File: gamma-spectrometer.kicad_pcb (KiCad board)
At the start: 2 copper layers, 123.5 x 49.5 mm, 79 parts, among them J1 *, J2 *, J3 20449-001E-03, J4 *, J5 20449-001E-03, J6 *, Q1 2N7002, Q2 2N7002, Q3 MMBT5088LT1G, Q4 MMBT5088LT1G, SW1 *, U1 Pico 2, U10 MICROFC-60035-SMT-TR1, U2 OPA357AIDBVR, U3 TLV3201AIDBVR, U4 OPA357AIDBVR, U5 OPA357AIDBVR, U6 LM4040AIM3-3.0+T, U7 LM4040AIM3-3.0+T, U8 MAX5026EUT_T, U9 TPS7B6950DBVR

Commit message: BDG4-01 module boards design
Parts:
- removed J3, J5: 20449-001E-03, 20449-001E-03:IPEX_20449-001E-03
- removed J4, J6: *, B2B-PH-K-S_LF__SN_:JST_B2B-PH-K-S(LF)(SN)
- removed LS1: AST0760MCTRQ (6kHz), AST0760MCTRQ:AST0760_MAL
- removed Q2: 2N7002, Package_TO_SOT_SMD:SOT-23
- removed SW1: *, SW_TL3305AF160QG:SW_TL3305AF160QG
- C10, C11, C12, C13, C14, C15, C16, C18, C4, C5, C6, C8, C9, D3, D5, FB2, FB3, L1, Q1, R10, R11, R12, R13, R14, R15, R16, R6, R9, U4, U5, U6, U8: moved to B.Cu
- R1: value 1k -> 210k
- R2: value 100R -> 1k
- R4: value 210k -> 1k; moved to B.Cu
- R5: value 1k -> 100R
- R7: value 1k -> 210k; moved to B.Cu
- R8: value 210k -> 1k
- VR1: value 5k -> 50k; footprint 3296W-1-502LF:TRIM_3296W-1-502LF -> 3296W-1-503LF:TRIM_3296W-1-503LF
- VR2: value 50k -> 5k; footprint 3296W-1-503LF:TRIM_3296W-1-503LF -> 3296W-1-502LF:TRIM_3296W-1-502LF
- moved VR1 38.9 mm to (155.0, 72.5), turned to 0 degrees
- moved C9 38.1 mm to (105.5, 84.1), turned to 180 degrees
- moved C10 36.5 mm to (105.5, 82.1), turned to 0 degrees
- moved U7 35.5 mm to (143.2, 79.2), turned to 90 degrees
- moved R3 35.0 mm to (154.2, 80.8), turned to -90 degrees
- moved R11 34.9 mm to (111.5, 85.5)
- moved JP2 33.7 mm to (120.5, 69.5), turned to 180 degrees
- moved R2 33.6 mm to (155.8, 80.8)
- moved U5 32.3 mm to (109.0, 81.8), turned to -90 degrees
- moved R1 32.2 mm to (152.8, 80.8)
- moved C8 31.6 mm to (111.5, 80.0), turned to -90 degrees
- moved R10 28.9 mm to (120.6, 84.2), turned to -90 degrees
- moved U2 28.6 mm to (147.2, 77.0), turned to 0 degrees
- moved D1 28.2 mm to (148.5, 80.8)
- moved D3 27.8 mm to (118.0, 83.4), turned to -90 degrees
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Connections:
- C11 pad 1: Net-(U8-VCC) -> Net-(D5-A)
- C6 pad 1: GND -> Net-(U3-IN-)
- C6 pad 2: VCC -> GND
- C7 pad 1: Net-(U3-IN-) -> GND
- C7 pad 2: GND -> VCC
- FB3 pad 1: Net-(U8-VCC) -> Net-(D5-A)
- L1 pad 2: Net-(U8-VCC) -> Net-(D5-A)
- R1 pad 1: GND -> ANODE_IN
- R1 pad 2: ANODE_IN -> VREF1
- R13 pad 1: VREF1 -> VREF
- R2 pad 1: ANODE_IN -> GND
- R2 pad 2: Net-(D1-COM) -> ANODE_IN
- R3 pad 2: VREF -> VREF1
- R4 pad 1: ANODE_IN -> GND
- R4 pad 2: VREF -> Net-(U2--IN)
- R5 pad 1: GND -> ANODE_IN
- R5 pad 2: Net-(U2--IN) -> Net-(D1-COM)
- R7 pad 1: Net-(D2-PadA) -> Net-(VR1-CW)
- R7 pad 2: INT -> Net-(R7-Pad2)
- R8 pad 1: Net-(VR2-CCW) -> Net-(D2-PadA)
- R8 pad 2: Net-(R8-Pad2) -> INT
- R9 pad 1: VREF1 -> VREF
- R9 pad 2: Net-(R8-Pad2) -> Net-(R7-Pad2)
- U1 pad 10: TCKR -> unconnected-(U1-GPIO7-Pad10)_1
- U1 pad 19: Net-(U1-GPIO14) -> unconnected-(U1-GPIO14-Pad19)_1
- U1 pad 35: VREF -> VREF1
- U1 pad 40: unconnected-(U1-VBUS-Pad40) -> VBUS
- U6 pad 1: VREF1 -> VREF
- U7 pad 1: VREF -> VREF1
- U8 pad 4: Net-(U8-VCC) -> Net-(D5-A)
- U8 pad 5: Net-(U8-VCC) -> Net-(D5-A)
- VR1 pad 1: SIG -> GND
- VR1 pad 2: SIG -> Net-(U3-IN-)
- VR1 pad 3: Net-(U2--IN) -> Net-(VR1-CW)
- VR2 pad 1: Net-(VR2-CCW) -> SIG
- VR2 pad 2: Net-(U3-IN-) -> SIG
- VR2 pad 3: GND -> Net-(U2--IN)
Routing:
- net GND: track 151.7 -> 49.2 mm
- net VREF1: track 14.2 -> 62.6 mm, vias 0 -> 1
- net PEAK: track 56.2 -> 13.6 mm
- net TCKR: track 35.5 -> 0.00 mm
- net VREF: track 34.5 -> 3.69 mm, vias 3 -> 0
- net GND1: track 29.1 -> 0.00 mm, vias 0 -> 2
- net RST: track 29.9 -> 7.38 mm, vias 1 -> 0
- net +5V: track 93.2 -> 72.4 mm, vias 1 -> 2
- net SIG: track 39.7 -> 59.5 mm
- net VCC: track 134.0 -> 153.5 mm, vias 1 -> 2
- net Net-(U8-VCC): track 19.5 -> 0.00 mm
- net Net-(Q4-B): track 5.79 -> 24.9 mm
- net Net-(D5-A): track 9.71 -> 28.3 mm
- net PS_IN: track 14.1 -> 31.9 mm, vias 0 -> 1
- net Net-(U2--IN): track 25.4 -> 13.7 mm
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- added copper zone on F.Cu, net GND
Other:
- board size 123.5 x 49.5 mm -> 145.3 x 36.5 mm
- board text added: "CS"
- board text added: "GND"
- board text added: "MicroUSB"
- board text added: "OpenGammaKit v0.1.0"
- board text added: "RX"
- board text added: "SCK"
- board text added: "SCL"
- board text added: "SDA"
- board text added: "TX"
- board text added: "UR1"
- board text added: "UR2"
- board text added: "VCC"
- board text added: "БДГ4-01-А"
- board text added: "БДГ4-01-Б"
- board text removed: "Module v0.0.8"
- board text removed: "U2"

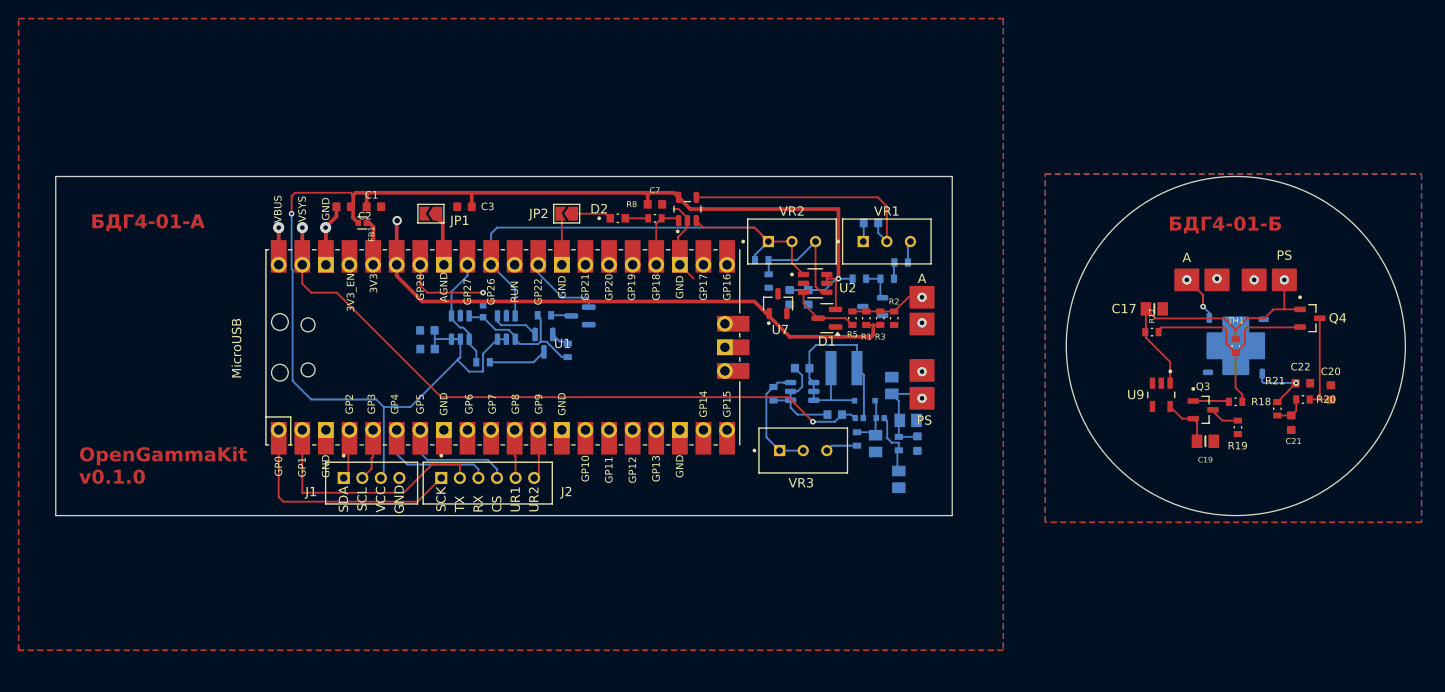
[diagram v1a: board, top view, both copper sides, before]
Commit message: PCB changes for more precise assembling
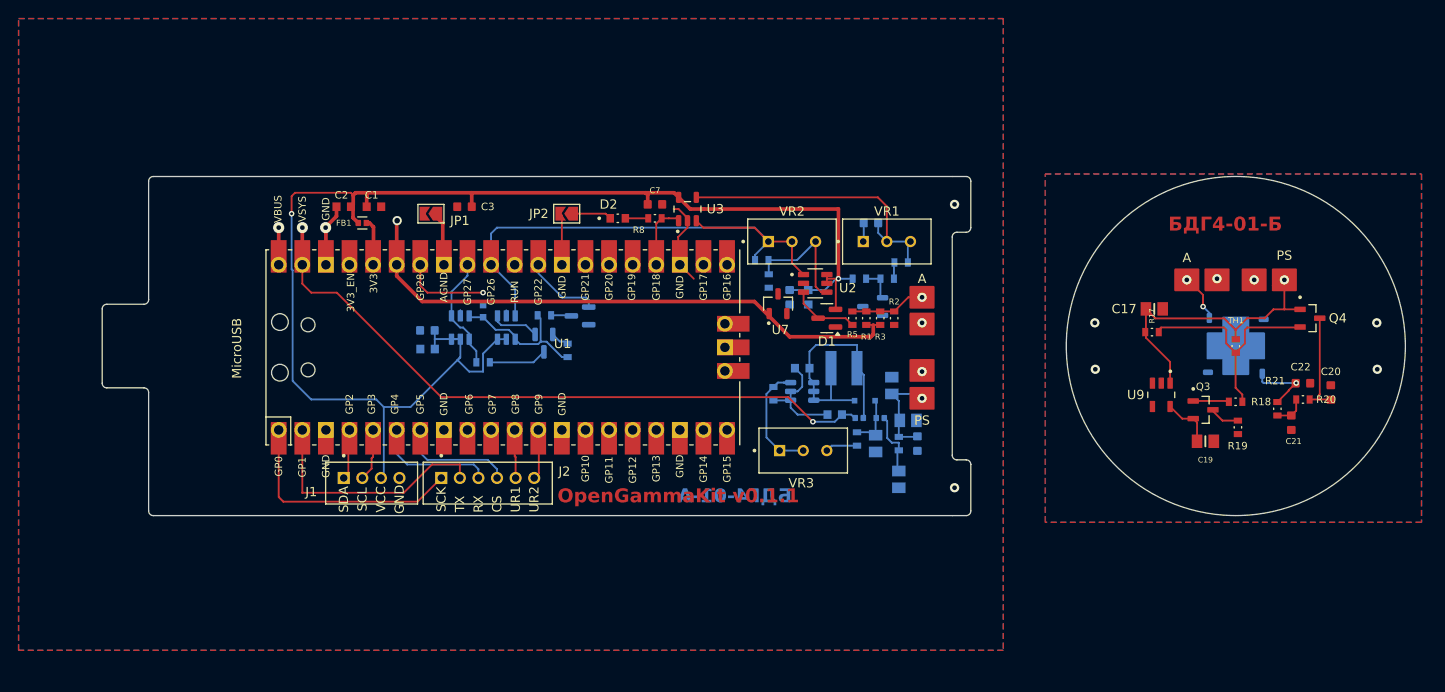
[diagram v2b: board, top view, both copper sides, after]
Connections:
- R7 pad 1: Net-(VR1-CW) -> Net-(U3-IN-)
- VR1 pad 3: Net-(VR1-CW) -> Net-(U3-IN-)
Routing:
- net Net-(U3-IN-): track 27.1 -> 32.0 mm
- net Net-(VR1-CW): track 2.36 -> 0.00 mm
- net GND1: vias 2 -> 6
- net GND: vias 4 -> 6
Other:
- board size 145.3 x 36.5 mm -> 140.3 x 36.5 mm
- board text added: "OpenGammaKit v0.1.1"
- board text removed: "OpenGammaKit v0.1.0"

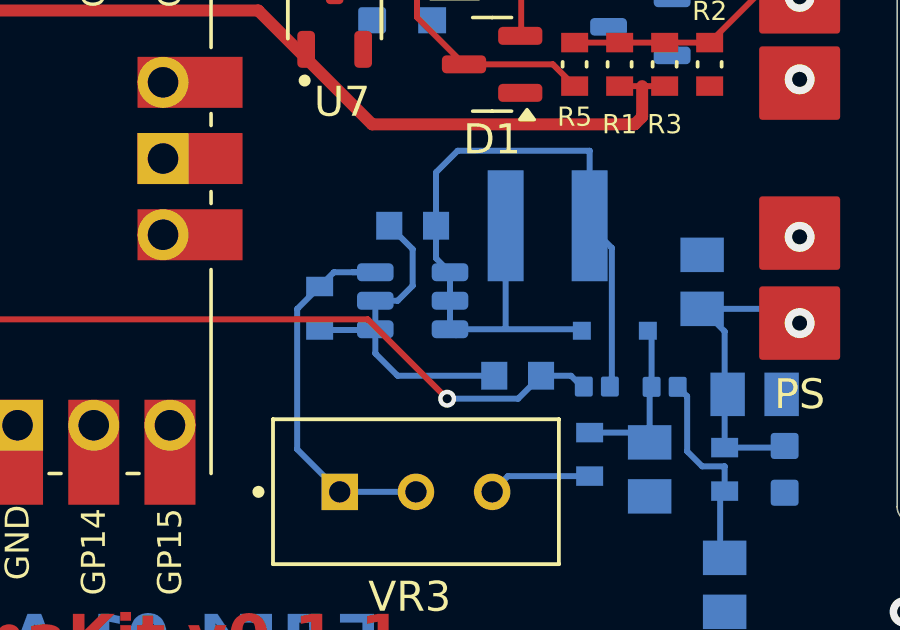
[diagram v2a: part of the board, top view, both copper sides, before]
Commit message: Important fix for SiPM power supply circuit. Moved gerber files.
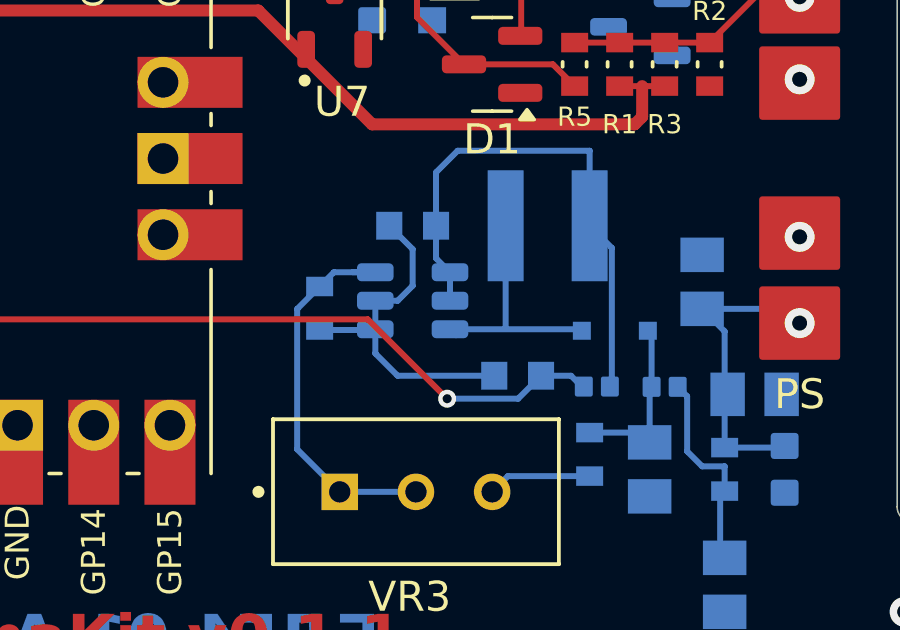
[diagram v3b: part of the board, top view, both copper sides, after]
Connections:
- C11 pad 1: Net-(D5-A) -> Net-(U8-VCC)
- FB3 pad 1: Net-(D5-A) -> Net-(U8-VCC)
- L1 pad 2: Net-(D5-A) -> Net-(U8-VCC)
- U8 pad 4: Net-(D5-A) -> Net-(U8-VCC)
- U8 pad 5: Net-(D5-A) -> Net-(U8-VCC)
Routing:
- net Net-(D5-A): track 28.3 -> 8.85 mm
- net Net-(U8-VCC): track 0.00 -> 18.5 mm
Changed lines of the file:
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@@
 			(drillshape 0)
 			(scaleselection 1)
-			(outputdirectory "gerber-files/")
+			(outputdirectory "fabrication-outputs/gerber-files/")
 		)
 	)
@@
 	(net 86 "unconnected-(U1-GPIO14-Pad19)_1")
 	(net 87 "VBUS")
+	(net 88 "Net-(U8-VCC)")
 	(footprint "3296W-1-503LF:TRIM_3296W-1-503LF"
 		(layer "F.Cu")
@@
 			(layers "B.Cu" "B.Paste" "B.Mask")
 			(roundrect_rratio 0.125)
-			(net 61 "Net-(D5-A)")
+			(net 88 "Net-(U8-VCC)")
 			(pintype "passive")
 			(solder_mask_margin 0.102)
@@
 			(size 0.87 0.93)
 			(layers "B.Cu" "B.Paste" "B.Mask")
-			(net 61 "Net-(D5-A)")
+			(net 88 "Net-(U8-VCC)")
 			(pintype "passive")
 			(solder_mask_margin 0.102)
@@
 			(layers "B.Cu" "B.Paste" "B.Mask")
 			(roundrect_rratio 0.25)
-			(net 61 "Net-(D5-A)")
+			(net 88 "Net-(U8-VCC)")
 			(pinfunction "~{SHDN}")
 			(pintype "input")
@@
 			(layers "B.Cu" "B.Paste" "B.Mask")
 			(roundrect_rratio 0.25)
-			(net 61 "Net-(D5-A)")
+			(net 88 "Net-(U8-VCC)")
 			(pinfunction "VCC")
 			(pintype "power_in")
@@
 			(size 1.2 3.7)
 			(layers "B.Cu" "B.Paste" "B.Mask")
-			(net 61 "Net-(D5-A)")
+			(net 88 "Net-(U8-VCC)")
 			(pintype "passive")
 			(solder_mask_margin 0.102)
@@
 	)
 	(segment
-		(start 146.63 87.215)
-		(end 147.095 87.68)
-		(width 0.2)
-		(layer "B.Cu")
-		(net 61)
-	)
-	(segment
-		(start 152.49 91.555)
-		(end 152.49 86.87)
-		(width 0.2)
-		(layer "B.Cu")
-		(net 61)
-	)
-	(segment
 		(start 148.95 86.13)
 		(end 148.95 89.48)
@@
 	)
 	(segment
-		(start 151.75 83.63)
-		(end 147.35 83.63)
-		(width 0.2)
-		(layer "B.Cu")
-		(net 61)
-	)
-	(segment
-		(start 147.095 87.68)
-		(end 147.4 87.68)
-		(width 0.2)
-		(layer "B.Cu")
-		(net 61)
-	)
-	(segment
-		(start 152.565 91.63)
-		(end 152.49 91.555)
-		(width 0.2)
-		(layer "B.Cu")
-		(net 61)
-	)
-	(segment
 		(start 147.095 89.58)
 		(end 151.44 89.58)
@@
 	)
 	(segment
-		(start 146.63 84.35)
-		(end 146.63 86.13)
-		(width 0.2)
-		(layer "B.Cu")
-		(net 61)
-	)
-	(segment
-		(start 147.35 83.63)
-		(end 146.63 84.35)
-		(width 0.2)
-		(layer "B.Cu")
-		(net 61)
-	)
-	(segment
-		(start 147.095 87.695)
-		(end 147.095 88.63)
-		(width 0.2)
-		(layer "B.Cu")
-		(net 61)
-	)
-	(segment
-		(start 146.63 86.13)
-		(end 146.63 87.215)
-		(width 0.2)
-		(layer "B.Cu")
-		(net 61)
-	)
-	(segment
 		(start 147.095 89.58)
 		(end 147.295 89.78)
@@
 	)
 	(segment
-		(start 151.75 86.13)
-		(end 151.75 83.63)
-		(width 0.2)
-		(layer "B.Cu")
-		(net 61)
-	)
-	(segment
-		(start 152.49 86.87)
-		(end 151.75 86.13)
-		(width 0.2)
-		(layer "B.Cu")
-		(net 61)
-	)
-	(segment
-		(start 147.095 88.63)
-		(end 147.095 89.58)
-		(width 0.2)
-		(layer "B.Cu")
-		(net 61)
-	)
-	(segment
-		(start 147.08 87.68)
-		(end 147.095 87.695)
-		(width 0.2)
-		(layer "B.Cu")
-		(net 61)
-	)
-	(segment
 		(start 153.75 91.565)
 		(end 153.815 91.5)
@@
 		(net 87)
 	)
+	(segment
+		(start 146.63 87.215)
+		(end 147.095 87.68)
+		(width 0.2)
+		(layer "B.Cu")
+		(net 88)
+	)
+	(segment
+		(start 152.49 91.555)
+		(end 152.49 86.87)
+		(width 0.2)
+		(layer "B.Cu")
+		(net 88)
+	)
+	(segment
+		(start 151.75 83.63)
+		(end 147.35 83.63)
+		(width 0.2)
+		(layer "B.Cu")
+		(net 88)
+	)
+	(segment
+		(start 147.095 87.68)
+		(end 147.4 87.68)
+		(width 0.2)
+		(layer "B.Cu")
+		(net 88)
+	)
+	(segment
+		(start 152.565 91.63)
+		(end 152.49 91.555)
+		(width 0.2)
+		(layer "B.Cu")
+		(net 88)
+	)
+	(segment
+		(start 146.63 84.35)
+		(end 146.63 86.13)
+		(width 0.2)
+		(layer "B.Cu")
+		(net 88)
+	)
+	(segment
+		(start 147.35 83.63)
+		(end 146.63 84.35)
+		(width 0.2)
+		(layer "B.Cu")
+		(net 88)
+	)
+	(segment
+		(start 147.095 87.695)
+		(end 147.095 88.63)
+		(width 0.2)
+		(layer "B.Cu")
+		(net 88)
+	)
+	(segment
+		(start 146.63 86.13)
+		(end 146.63 87.215)
+		(width 0.2)
+		(layer "B.Cu")
+		(net 88)
+	)
+	(segment
+		(start 151.75 86.13)
+		(end 151.75 83.63)
+		(width 0.2)
+		(layer "B.Cu")
+		(net 88)
+	)
+	(segment
+		(start 152.49 86.87)
+		(end 151.75 86.13)
+		(width 0.2)
+		(layer "B.Cu")
+		(net 88)
+	)
+	(segment
+		(start 147.08 87.68)
+		(end 147.095 87.695)
+		(width 0.2)
+		(layer "B.Cu")
+		(net 88)
+	)
 	(zone

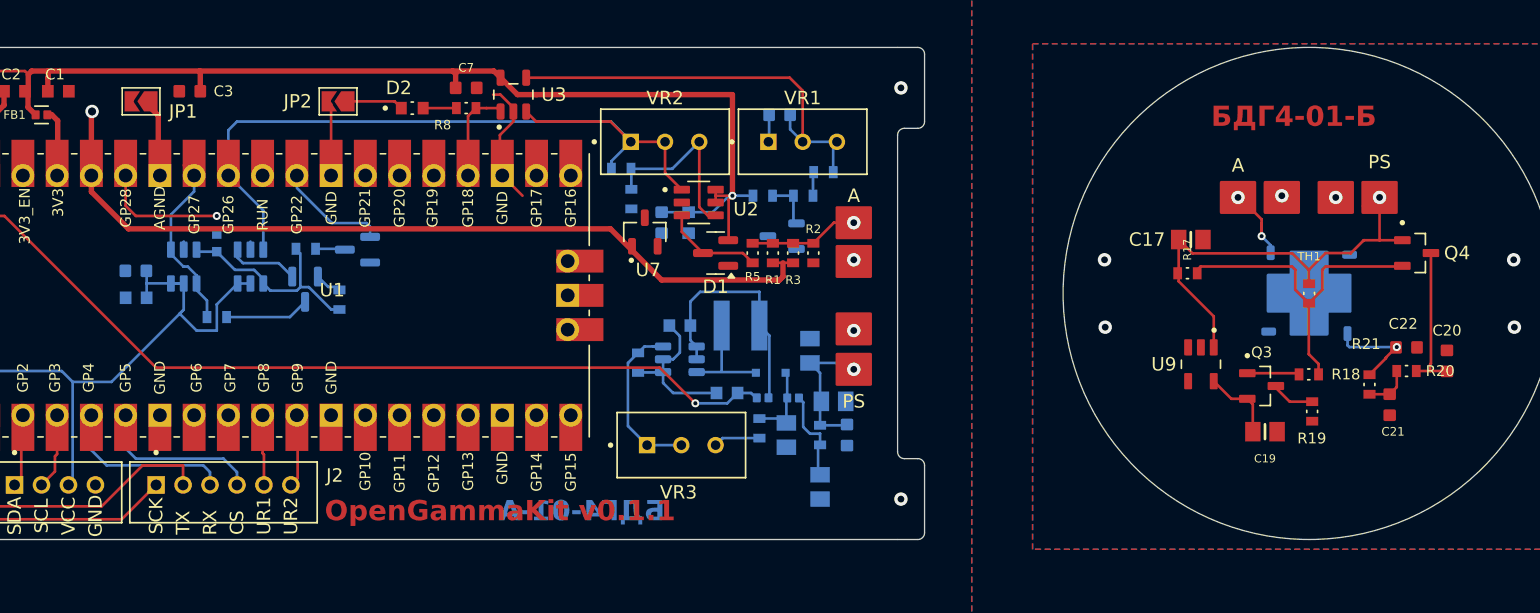
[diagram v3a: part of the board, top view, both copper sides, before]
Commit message: Updated BOM, schematic , foortprints, symbols
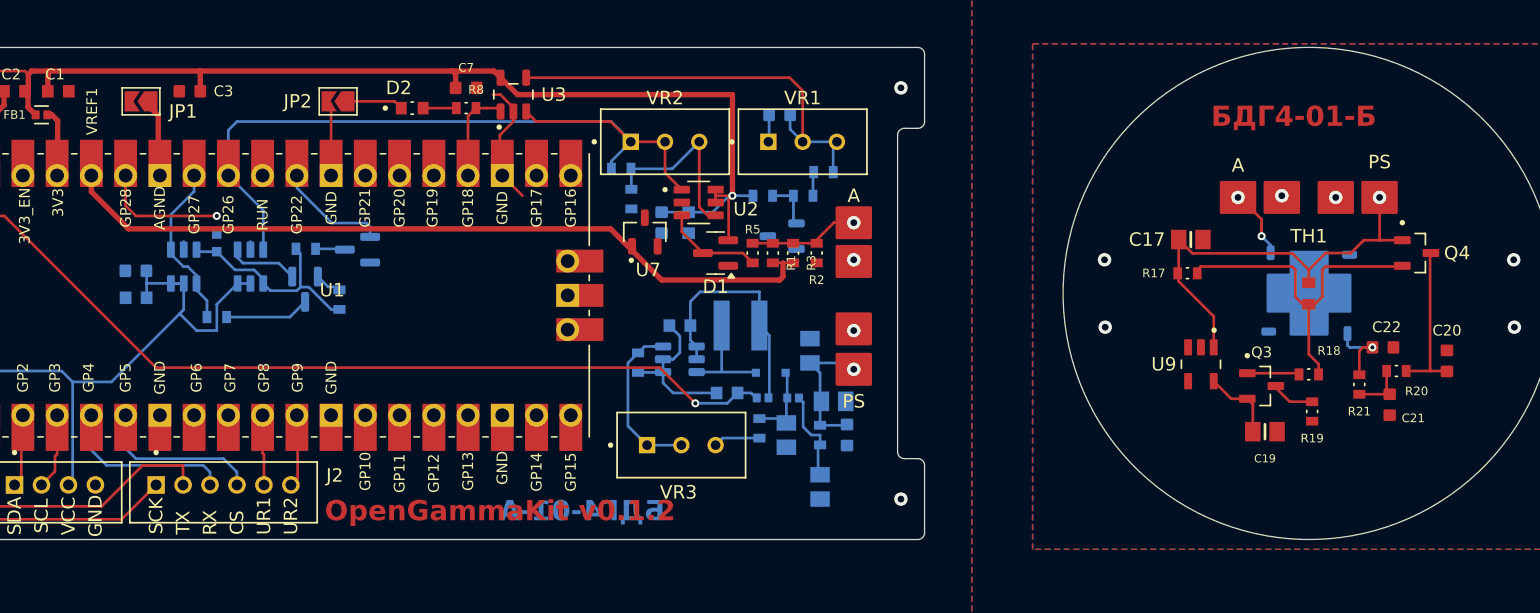
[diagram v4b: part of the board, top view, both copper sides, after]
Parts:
- R10, R16, R5: footprint ERJ3EKF2103V:RES_ERJ3EKF2103V -> ERJ3EKF1000V:RES_ERJ3EKF1000V
- R11, R14: footprint ERJ3EKF2103V:RES_ERJ3EKF2103V -> ERJ3EKF1002V:RES_ERJ3EKF1002V
- R12, R13, R2, R4, R8: footprint ERJ3EKF2103V:RES_ERJ3EKF2103V -> ERJ3EKF1001V:RES_ERJ3EKF1001V
- R17, R18, R19: footprint ERJ3EKF2103V:RES_ERJ3EKF2103V -> ERJ3EKF4992V:RES_ERJ3EKF4992V
- R20, R21: footprint ERJ3EKF2103V:RES_ERJ3EKF2103V -> ERJ3EKF49R9V:RES_ERJ3EKF49R9V
- R6: footprint ERJ3EKF2103V:RES_ERJ3EKF2103V -> ERJ3EKF2101V:RES_ERJ3EKF2101V
- TH1: footprint ERJ3EKF2103V:RES_ERJ3EKF2103V -> NTCS0603E3103FLT:NTCS0603E3103FLT
- moved C22 1.75 mm to (198.0, 87.8)
- moved R20 0.75 mm to (199.0, 89.5)
- moved R21 0.75 mm to (196.2, 90.5)
- moved R2 0.25 mm to (156.0, 80.8)
- turned TH1 to 90 degrees
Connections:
- TH1 pad 1: PS_IN -> Net-(Q4-B)
- TH1 pad 2: Net-(Q4-B) -> PS_IN
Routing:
- net VREF1: track 62.6 -> 57.8 mm, vias 1 -> 0
- net Net-(C22-Pad2): track 7.42 -> 5.63 mm
- net Net-(Q4-E): track 11.1 -> 11.8 mm
- net Net-(C21-Pad2): track 3.44 -> 4.07 mm
- net Net-(Q4-B): track 24.9 -> 25.6 mm
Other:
- board text added: "OpenGammaKit v0.1.2"
- board text added: "VREF1"
- board text removed: "OpenGammaKit v0.1.1"
